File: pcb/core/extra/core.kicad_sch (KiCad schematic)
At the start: 7 parts, among them J1 Conn_01x11, J2 Conn_01x11, U1 Helios

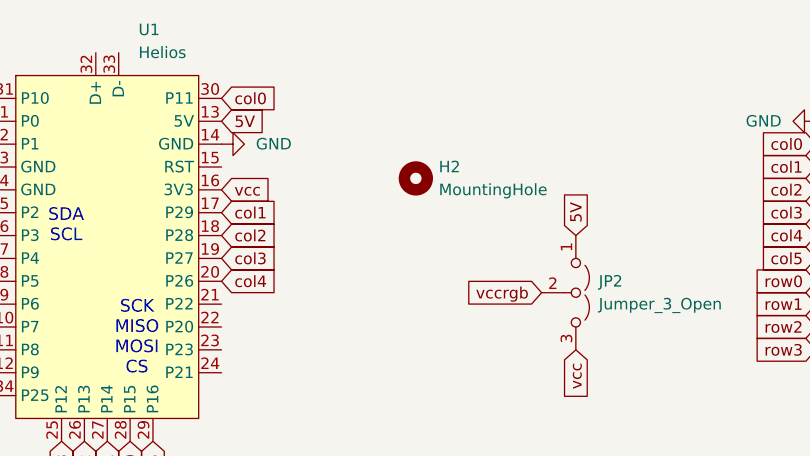
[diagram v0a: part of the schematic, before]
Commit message: moved rgb jumpers to the other side
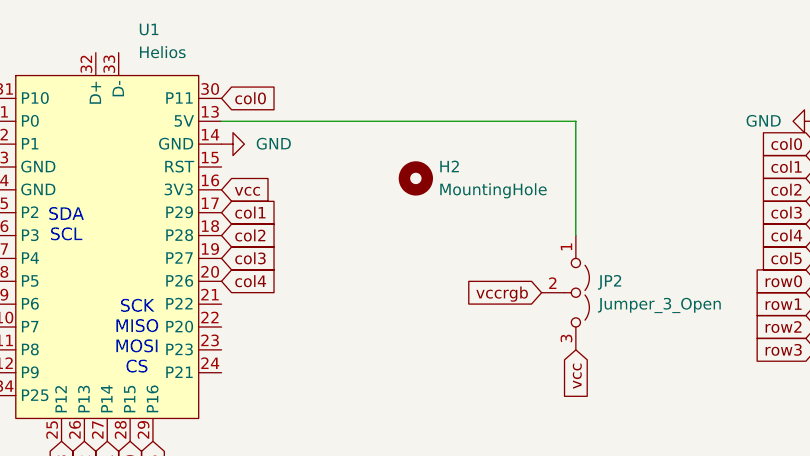
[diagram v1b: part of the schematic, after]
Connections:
- net 5V: no longer names the net of JP2.1 (A), U1.13 (5V)

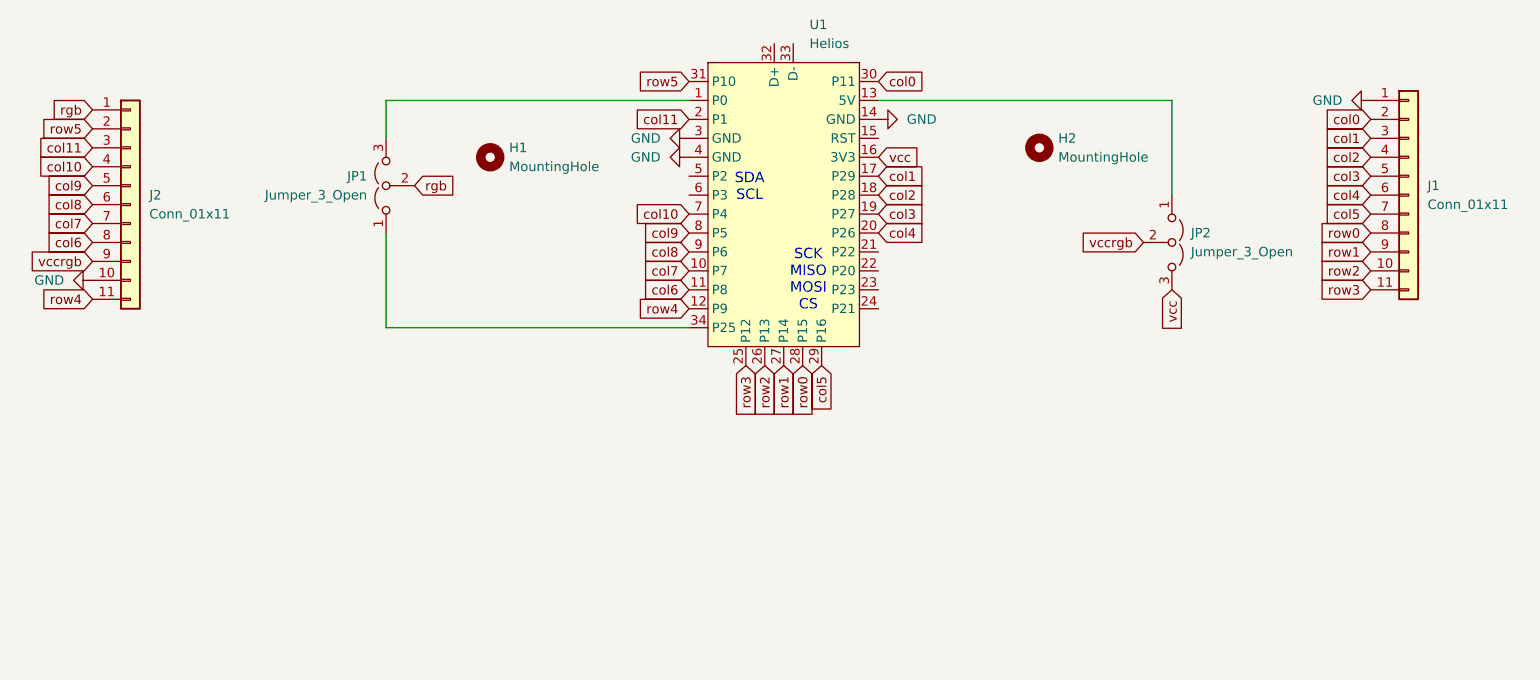
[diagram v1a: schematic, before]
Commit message: finished extra core pcb
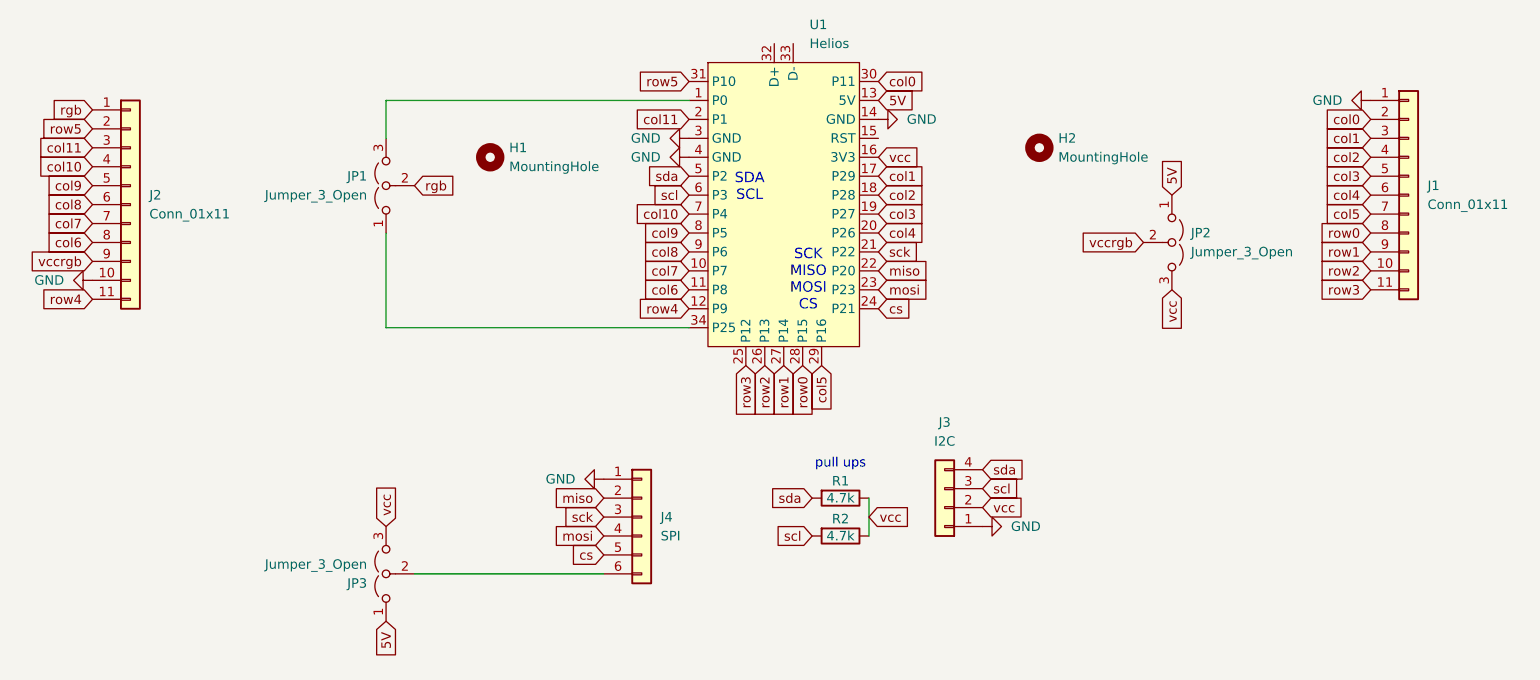
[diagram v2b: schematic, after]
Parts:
- added J3: I2C, Connector_PinHeader_2.54mm:PinHeader_1x04_P2.54mm_Vertical, symbol Connector_Generic:Conn_01x04
- added J4: SPI, Connector_PinHeader_2.54mm:PinHeader_1x06_P2.54mm_Vertical, symbol Connector_Generic:Conn_01x06
- added JP3: Jumper_3_Open, Jumper:SolderJumper-3_P1.3mm_Open_RoundedPad1.0x1.5mm, symbol Jumper:Jumper_3_Open
- added R1, R2: 4.7k, Resistor_THT:R_Axial_DIN0207_L6.3mm_D2.5mm_P7.62mm_Horizontal, symbol Device:R
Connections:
- net GND: now also J3.1 (Pin_1), J4.1 (Pin_1)
- net vcc: now also J3.2 (Pin_2), JP3.3 (B), R1.1, R2.1
- net 5V: now reaches JP2.1 (A), U1.13 (5V)
- net 5V: now also JP3.1 (A)
- net sck: now reaches U1.21 (P22)
- net sck: now also J4.3 (Pin_3)
- net miso: now reaches U1.22 (P20)
- net miso: now also J4.2 (Pin_2)
- net mosi: now reaches U1.23 (P23)
- net mosi: now also J4.4 (Pin_4)
- net cs: now reaches U1.24 (P21)
- net cs: now also J4.5 (Pin_5)
- net sda: now reaches U1.5 (P2)
- net sda: now also J3.4 (Pin_4), R1.2
- net scl: now reaches U1.6 (P3)
- net scl: now also J3.3 (Pin_3), R2.2
- new net: J4.6 (Pin_6), JP3.2 (C)
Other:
- note added: "pull ups"
